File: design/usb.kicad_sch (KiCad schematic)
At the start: 19 parts, among them J4 USB_B_Mini, U7 USBLC6-2SC6, U8 FT231XS

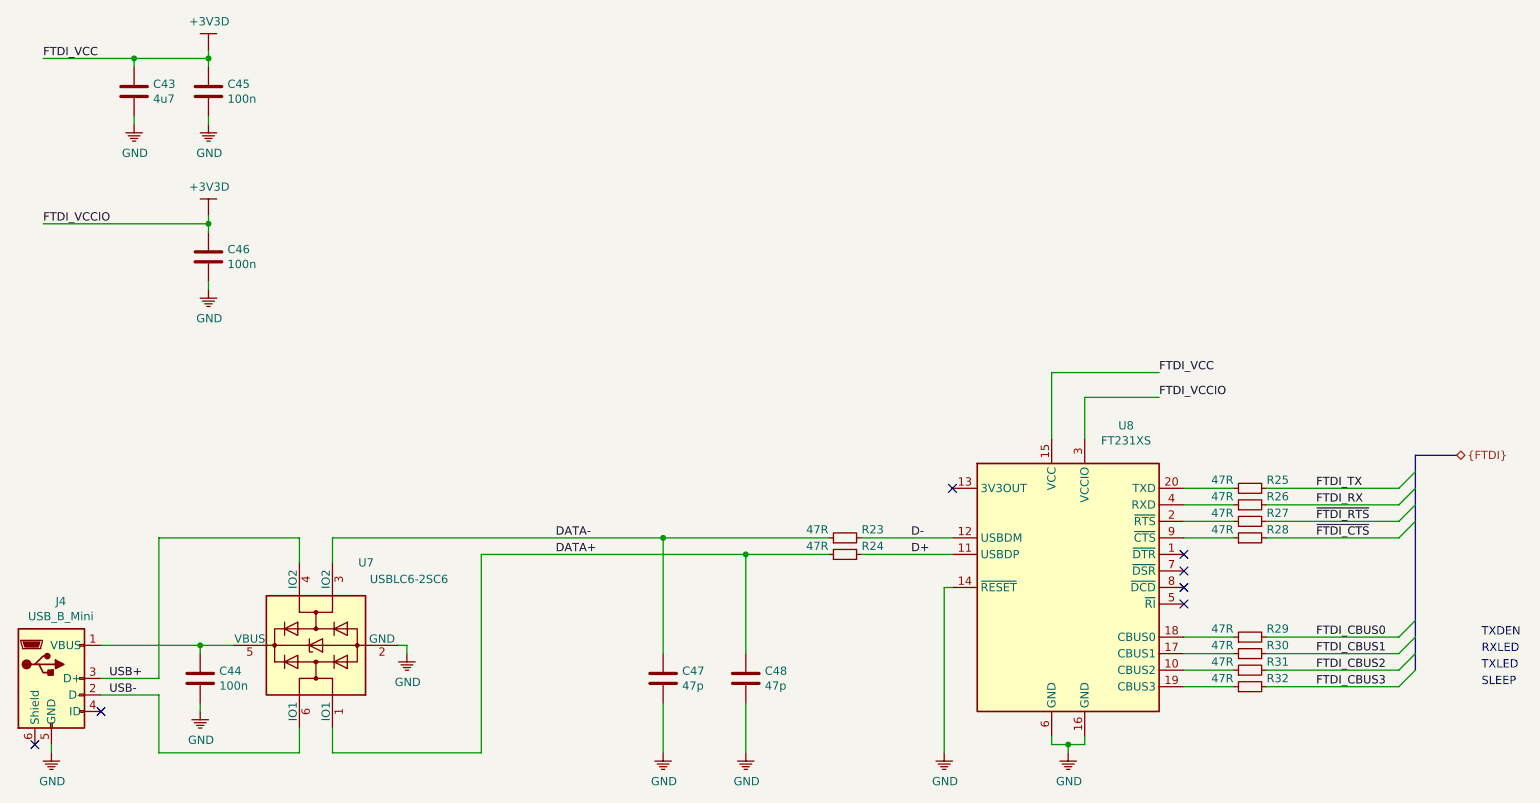
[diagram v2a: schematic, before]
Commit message: Added FTDI placemnt
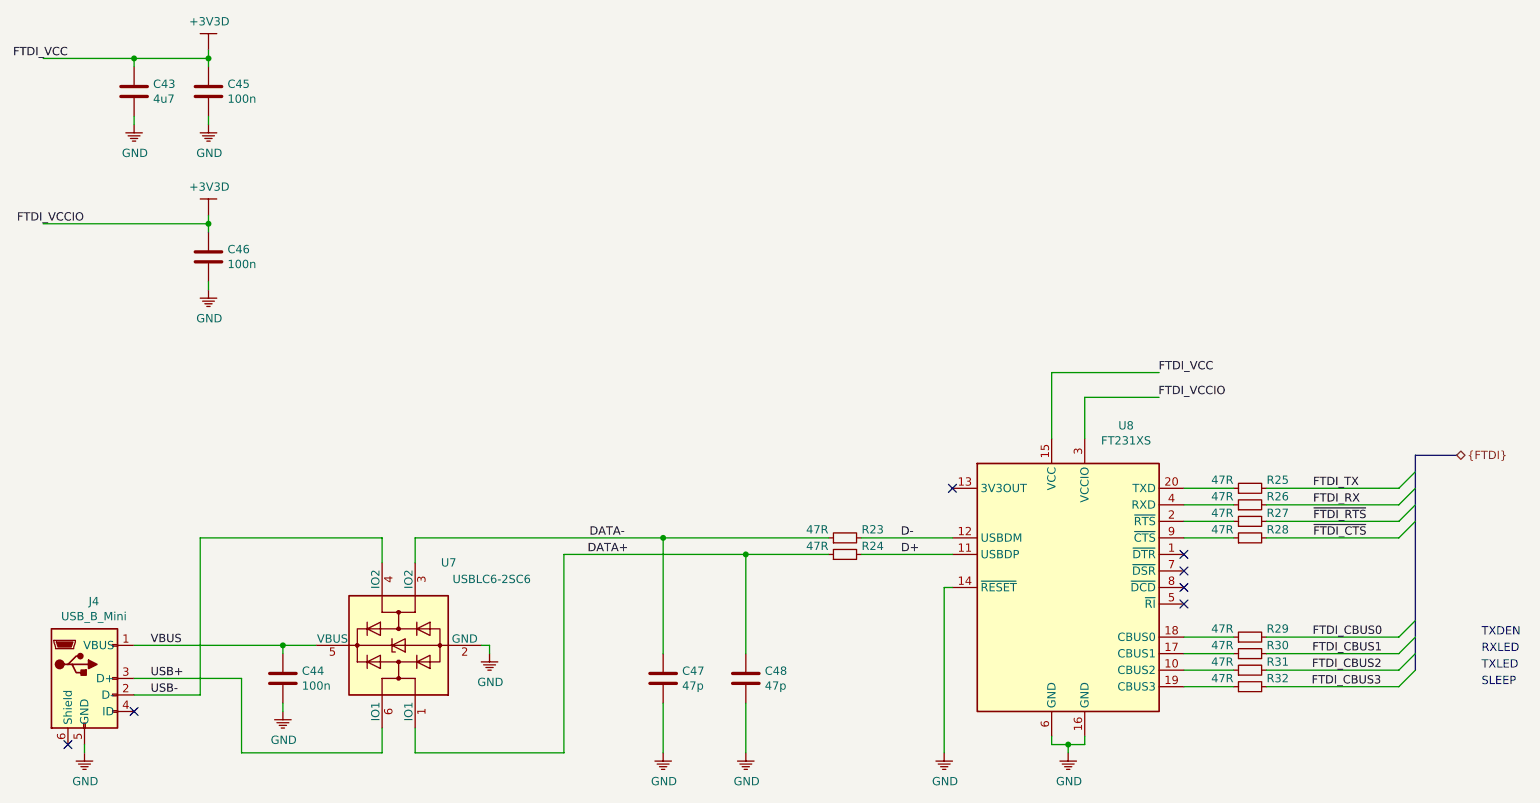
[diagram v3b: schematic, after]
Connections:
- net +3V3D: no longer U8.15 (VCC), U8.3 (VCCIO)
- net USB+: now also U7.6 (IO1); no longer U7.4 (IO2)
- net USB-: now also U7.4 (IO2); no longer U7.6 (IO1)
- net VBUS: now reaches C44.1, J4.1 (VBUS), U7.5 (VBUS)
- new net FTDI_VCC: U8.15 (VCC)
- new net FTDI_VCCIO: U8.3 (VCCIO)
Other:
- moved on the sheet: C44, J4, U7

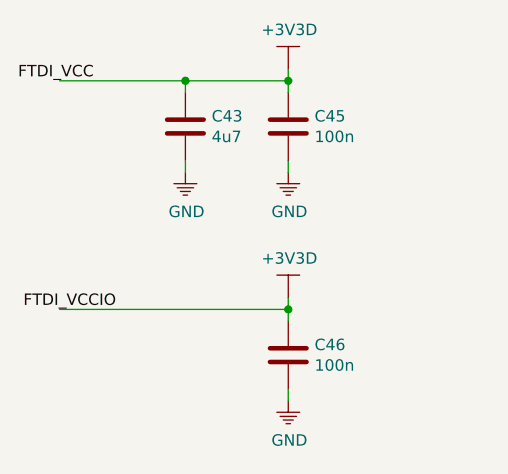
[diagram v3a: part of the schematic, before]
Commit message: Added MCU placement
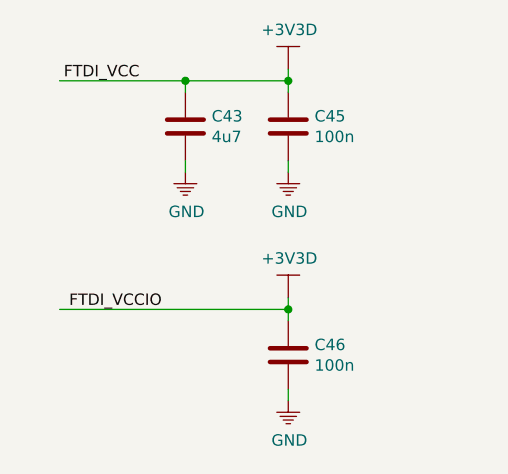
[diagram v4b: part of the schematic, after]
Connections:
- net FTDI_VCC is gone; now on net +3V3D: U8.15 (VCC)
- net FTDI_VCCIO is gone; now on net +3V3D: U8.3 (VCCIO)
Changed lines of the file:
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@@
     (effects (font (size 1.27 1.27)) (justify left bottom))
   )
-  (label "FTDI_VCC" (at 25.85 29.21 0)
+  (label "FTDI_VCC" (at 30.93 29.21 0)
     (effects (font (size 1.27 1.27)) (justify left bottom))
   )
-  (label "FTDI_VCCIO" (at 26.445 54.61 0)
+  (label "FTDI_VCCIO" (at 31.525 54.61 0)
     (effects (font (size 1.27 1.27)) (justify left bottom))
   )
